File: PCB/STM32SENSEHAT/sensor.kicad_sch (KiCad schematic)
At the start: 7 parts, among them U4 BME280

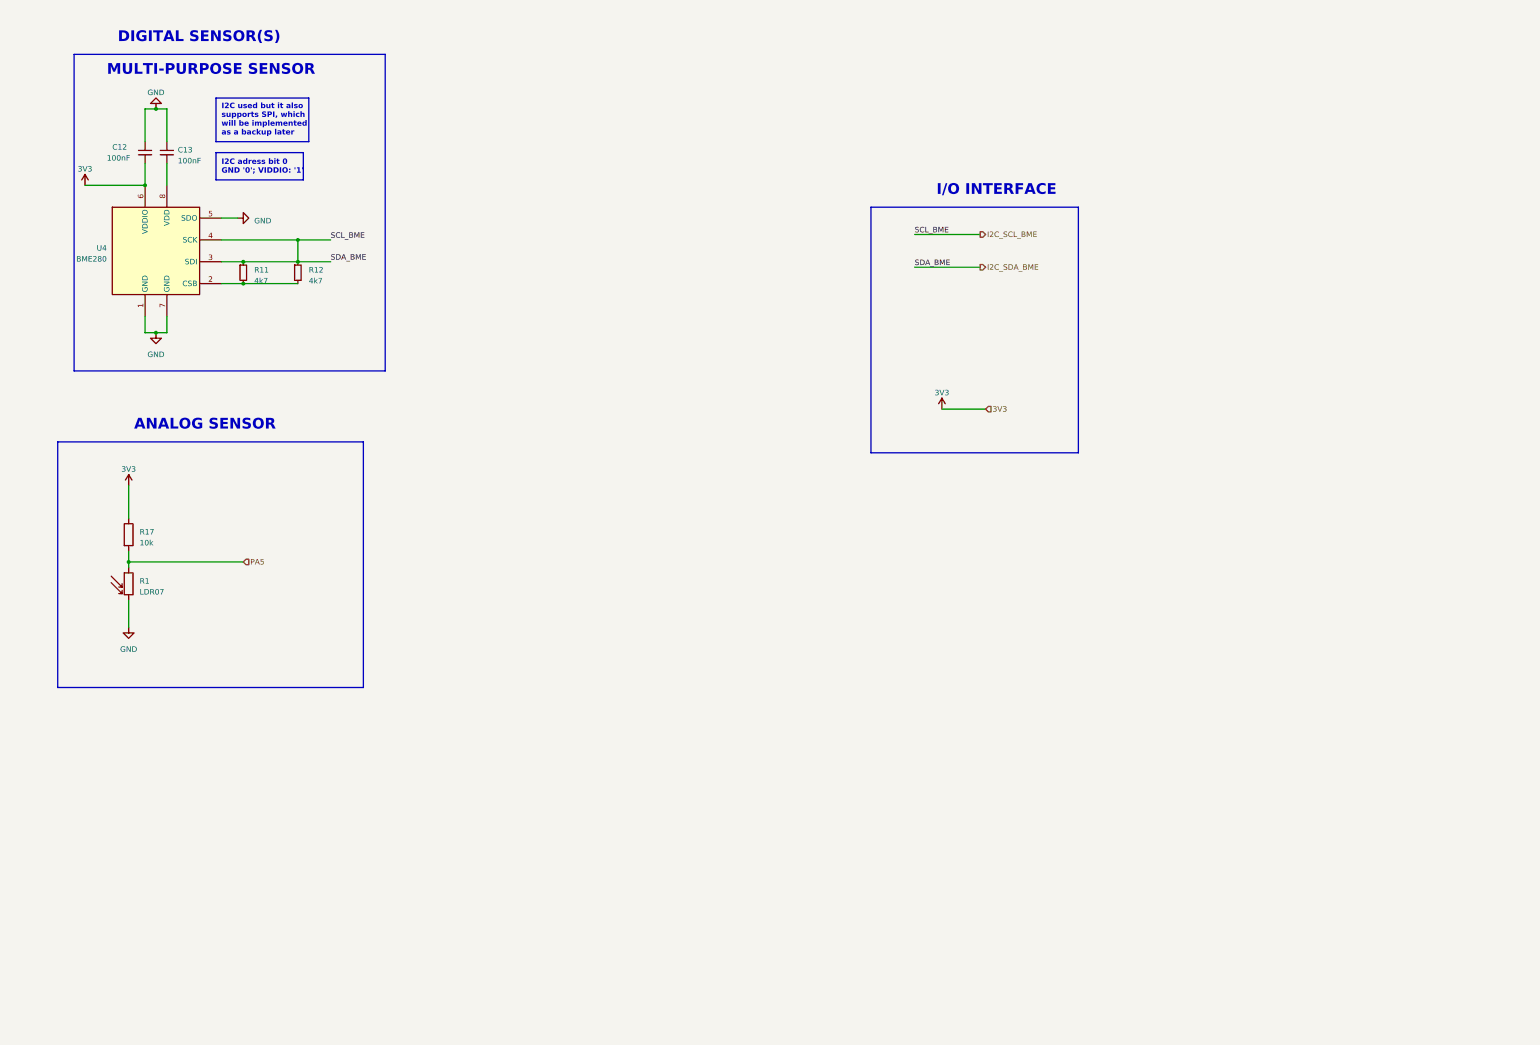
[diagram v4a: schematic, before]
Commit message: Added an extra back up sensor(#LTR-303 ALS-01),Test points for I2C SDA and SCL and solder jumpers
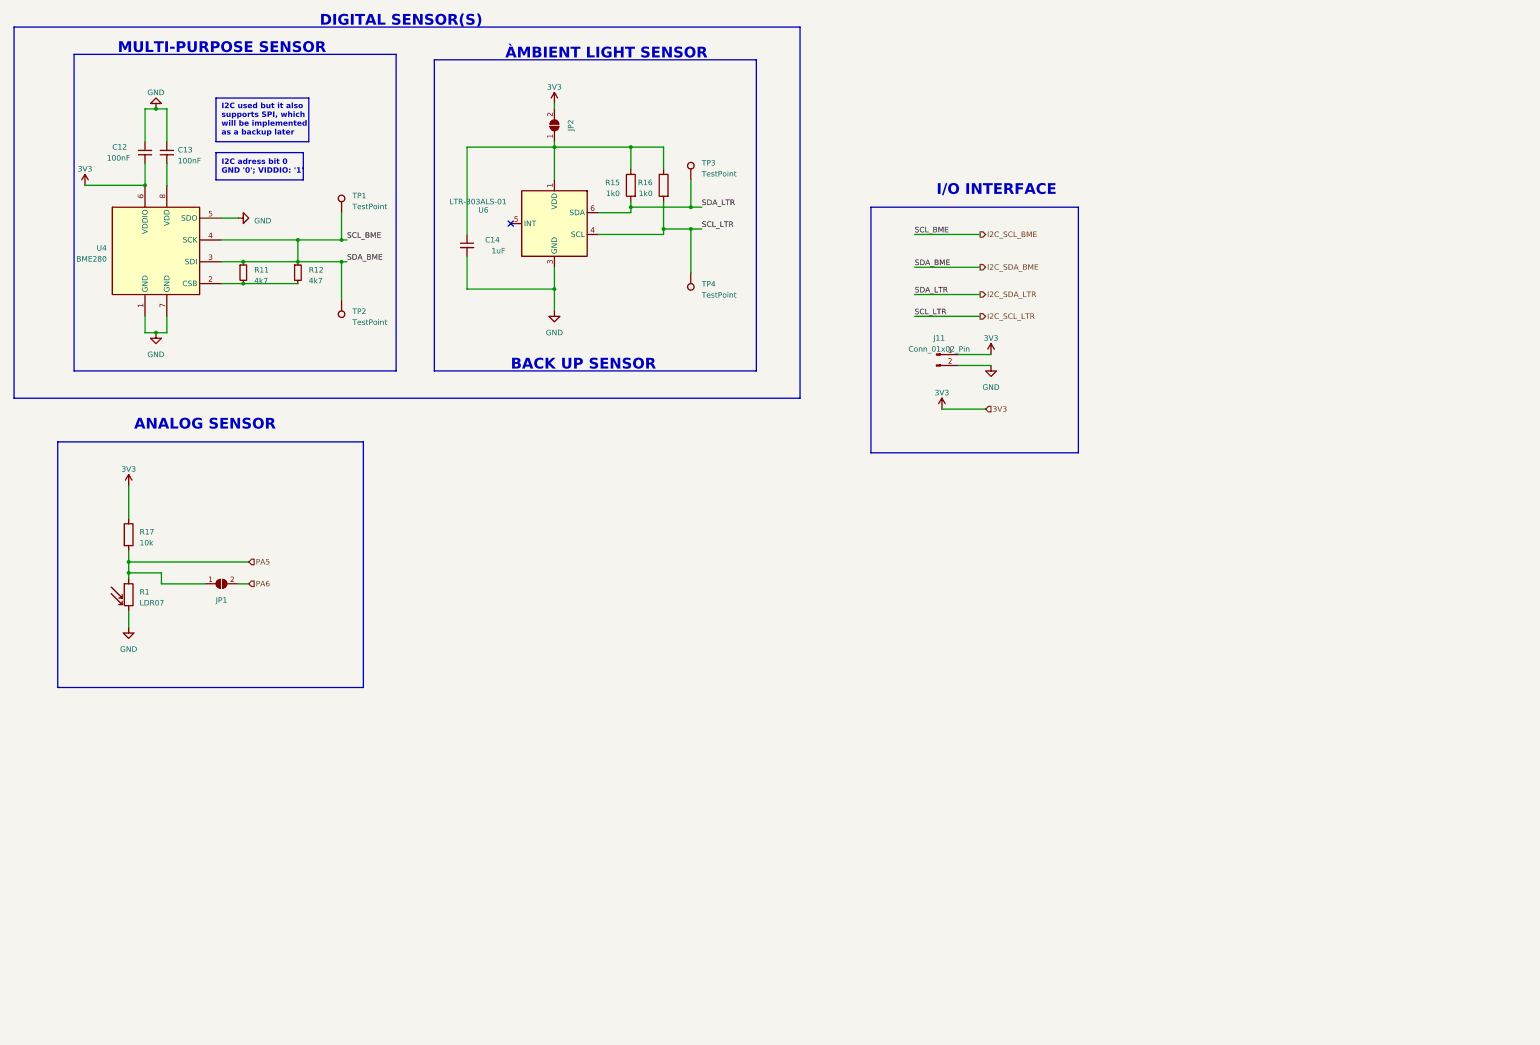
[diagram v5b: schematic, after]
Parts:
- added C14: 1uF, symbol Device:C_Small
- added J11: Conn_01x02_Pin, symbol Connector:Conn_01x02_Pin
- added JP1, JP2: SolderJumper_2_Open, symbol Jumper:SolderJumper_2_Open
- added R15, R16: 1k0, symbol Device:R
- added TP1, TP2, TP3, TP4: TestPoint, symbol Connector:TestPoint
- added U6: LTR-303ALS-01, OptoDevice:Lite-On_LTR-303ALS-01, symbol Sensor_Optical:LTR-303ALS-01
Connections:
- net GND: now also C14.2, J11.2 (Pin_2), U6.3 (GND)
- net I2C_SCL_BME: now also TP1.1, TP2.1
- net PA5: now also JP1.1 (A)
- net VCC: now also J11.1 (Pin_1), JP2.2 (B)
- new net: C14.1, JP2.1 (A), R15.1, R16.1, U6.1 (VDD)
- new net I2C_SCL_LTR: R16.2, TP4.1, U6.4 (SCL)
- new net I2C_SDA_LTR: R15.2, TP3.1, U6.6 (SDA)
- new net PA6: JP1.2 (B)
- no-connect marks 0 -> 1
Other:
- note added: "BACK UP SENSOR"
- note added: "ÀMBIENT LIGHT SENSOR"
- moved on the sheet: R1

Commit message: Protectuion features added to all schematica
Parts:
- added C18, C19: 100nF, symbol Device:C_Small
- added J10: Conn_01x01_Pin, symbol Connector:Conn_01x01_Pin
- added J12, J13: Conn_01x04_Pin, symbol Connector:Conn_01x04_Pin
- added R14, R18, R19, R20, R21, R22, R23, R24, R25, R26, R27, R28: 0R, symbol Device:R_Small
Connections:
- net GND: now also C18.2, C19.2, J12.1 (Pin_1), J13.3 (Pin_3), R22.1, R22.2, R23.1, R23.2, R24.2, R28.1; no longer U4.5 (SDO), U6.3 (GND)
- net I2C_SCL_BME: now also R14.2, R18.2; no longer U4.3 (SDI), U4.4 (SCK)
- net I2C_SCL_LTR: now also R25.2; no longer U6.4 (SCL)
- net I2C_SDA_LTR: now also R26.2; no longer U6.6 (SDA)
- net at R11.2, R12.2: now also R19.2; no longer U4.2 (CSB)
- net at C13.2: now also R21.2; no longer U4.8 (VDD)
- net at C14.1, JP2.1 (A), R15.1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: now also R27.2; no longer U6.1 (VDD)
- net PA6: no longer names the net of JP1.2 (B)
- net PA6: now also J10.1 (Pin_1)
- net VCC renamed 3V3
- net 3V3: now also U4.8 (VDD), C18.1, C19.1, J13.2 (Pin_2), J13.4 (Pin_4), R20.1, R20.2, R21.1
- new net: R26.1, U6.6 (SDA)
- new net: R27.1, U6.1 (VDD)
- new net: R28.2, U6.3 (GND)
- new net: R25.1, U6.4 (SCL)
- new net CS_BME: J12.2 (Pin_2), R19.1, U4.2 (CSB)
- new net MISO_BME: J12.3 (Pin_3), R18.1, U4.3 (SDI)
- new net MOSI_BME: J13.1 (Pin_1), R24.1, U4.5 (SDO)
- new net SCLK_BME: J12.4 (Pin_4), R14.1, U4.4 (SCK)
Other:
- note added: "I2C used but it also supports SPI, which is implemented as a backup"
- note added: "SPI-BACK UP"
- note removed: "I2C used but it also supports SPI, which will be implemented as a backup later"
- moved on the sheet: C12, C13, C14, J11, JP1, JP2, R1, R11, R12, R15, R16, R17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

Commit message: Schematics reviewed
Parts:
- J10: footprint (none) -> Connector_PinHeader_2.54mm:PinHeader_1x01_P2.54mm_Vertical
- J11: footprint (none) -> Connector_PinHeader_2.54mm:PinHeader_1x02_P2.54mm_Vertical
- J12, J13: footprint (none) -> Connector_PinHeader_2.54mm:PinHeader_1x04_P2.54mm_Vertical
- JP1: footprint (none) -> Jumper:SolderJumper-2_P1.3mm_Open_RoundedPad1.0x1.5mm
- JP2: footprint (none) -> Jumper:SolderJumper-2_P1.3mm_Open_Pad1.0x1.5mm
- TP1, TP2, TP3, TP4: footprint (none) -> TestPoint:TestPoint_Pad_D3.0mm
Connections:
- net 3V3: now also R21.2; no longer C12.2, R20.1, R21.1, U4.6 (VDDIO), U4.8 (VDD)
- net CS_BME: no longer R19.1, U4.2 (CSB)
- net GND: no longer R22.2, R23.2, U4.1 (GND), U4.7 (GND)
- net I2C_SCL_BME: no longer R11.1, R18.2, TP2.1
- net MISO_BME: no longer R18.1, U4.3 (SDI)
- net MOSI_BME: no longer R24.1, U4.5 (SDO)
- net SCLK_BME: no longer R14.1, U4.4 (SCK)
- net at R11.2, R12.2, R19.2: now also C12.2, R20.1, U4.6 (VDDIO)
- net at C13.2: now also R21.1, U4.8 (VDD); no longer R21.2
- new net: R19.1, U4.2 (CSB)
- new net: R18.1, U4.3 (SDI)
- new net: R14.1, U4.4 (SCK)
- new net: R24.1, U4.5 (SDO)
- new net 1: R22.2, U4.1 (GND)
- new net 7: R23.2, U4.7 (GND)
- new net I2C_SDA_BME: R11.1, R18.2, TP2.1
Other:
- note added: "5"
- note added: "6"
- note added: "7"
- note added: "8"
- moved on the sheet: R18

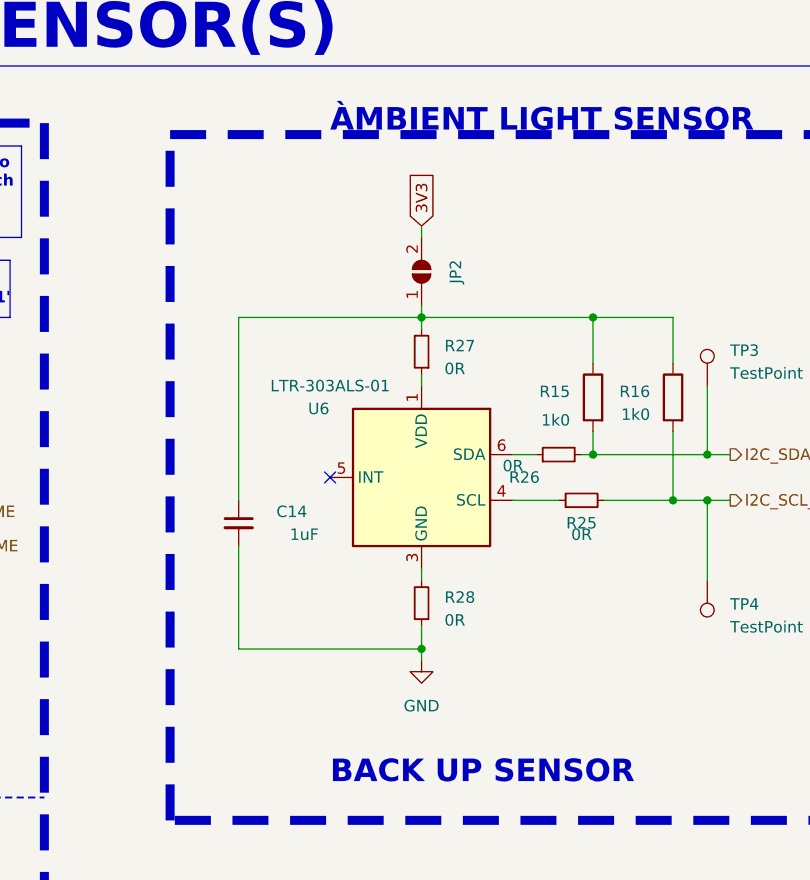
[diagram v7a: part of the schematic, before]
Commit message: Added footprints to the components but still pending review by Rumbizdai and Phomolo
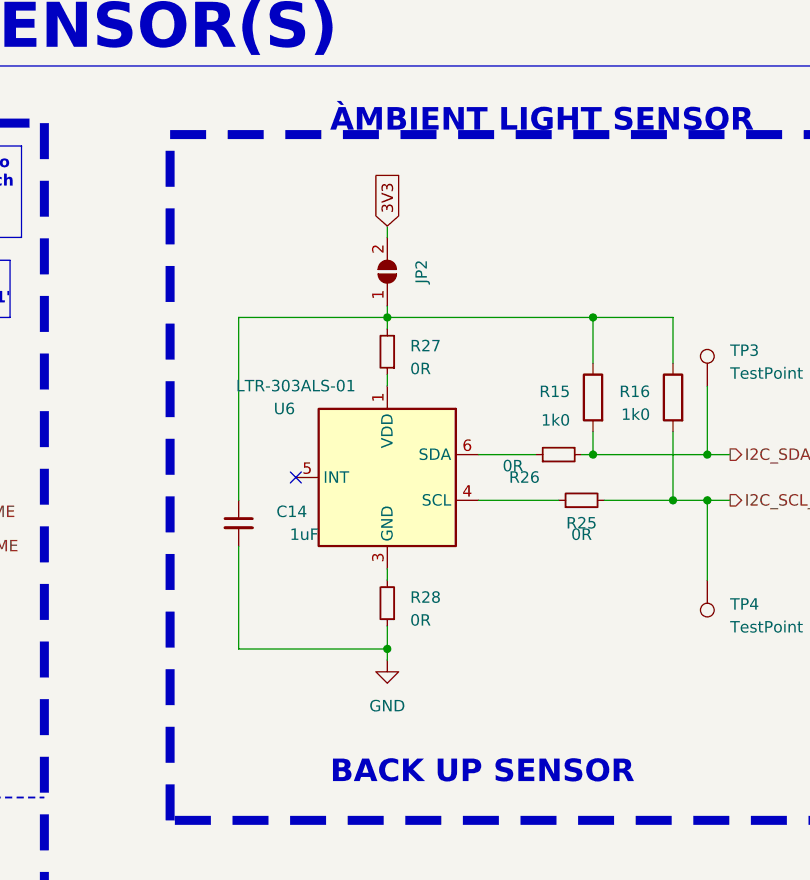
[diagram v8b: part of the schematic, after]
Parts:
- C12, C13, C14, C18, C19: footprint (none) -> Capacitor_SMD:C_0805_2012Metric
- R11, R12, R14, R17, R18, R19, R20, R21, R22, R23, R24, R25, R26, R27, R28: footprint (none) -> Resistor_SMD:R_0805_2012Metric
- R15, R16: footprint (none) -> Resistor_SMD:R_0603_1608Metric
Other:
- moved on the sheet: JP2, R27, R28, U6
